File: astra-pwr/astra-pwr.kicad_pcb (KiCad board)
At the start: 2 copper layers, 66.4 x 44 mm, 45 parts, among them J1 12V_IN, J2 RPI_PWR, J3 MISC_OUT, J4 STATUS_LED, U1 LMR54410DBVR, U2 TPS563240DDC, U3 LM321MF, U4 LM321MF, U5 LM321MF

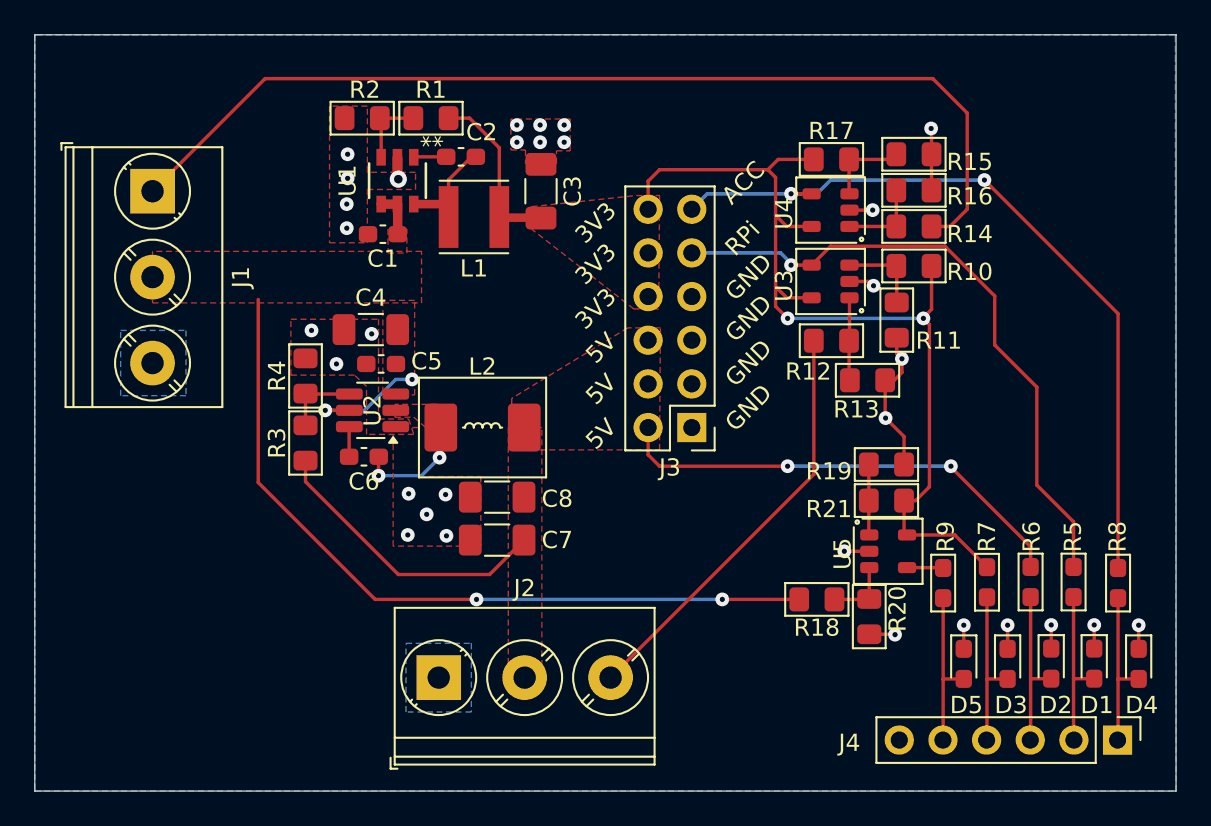
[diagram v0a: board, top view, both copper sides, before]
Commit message: Touchups on power board size
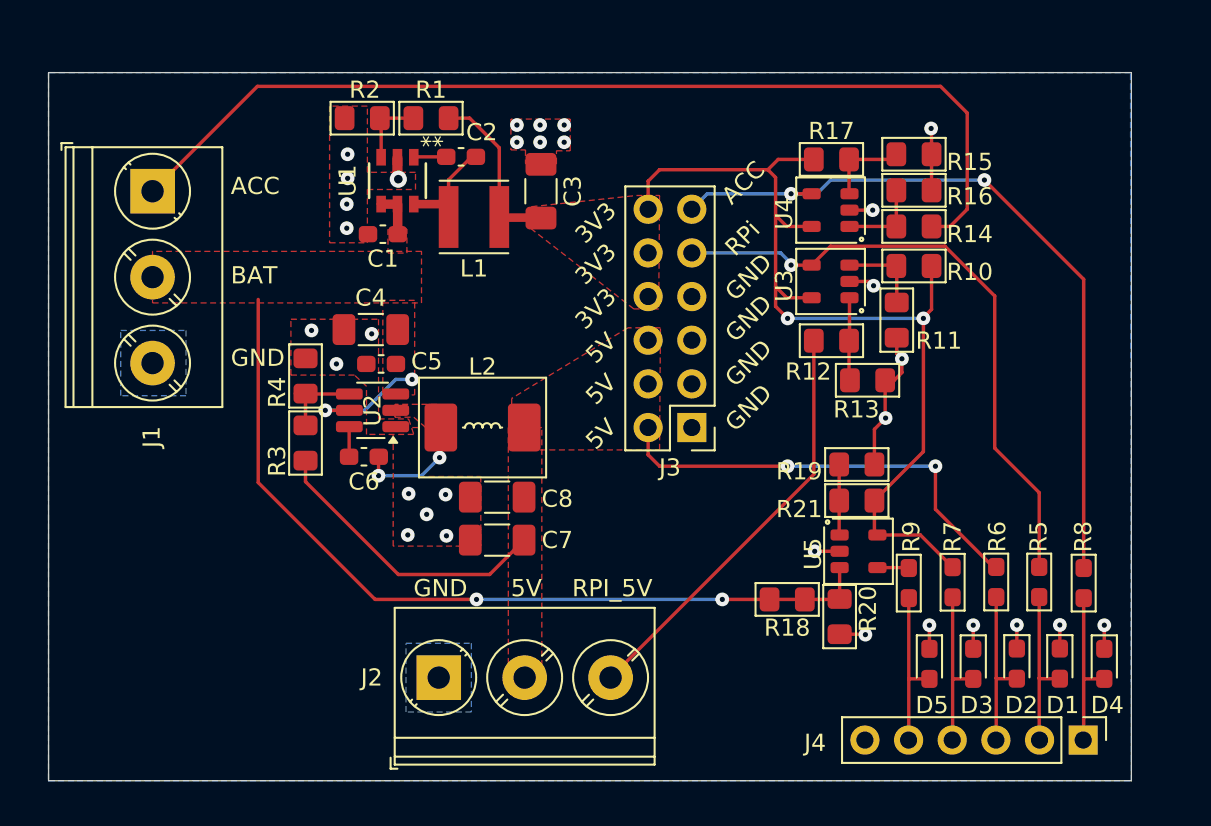
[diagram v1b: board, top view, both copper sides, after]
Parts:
- moved D1 2.00 mm to (97.2, 75.8)
- moved D2 2.00 mm to (94.7, 75.8)
- moved D3 2.00 mm to (92.2, 75.8)
- moved D4 2.00 mm to (99.8, 75.8)
- moved D5 2.00 mm to (89.7, 75.8)
- moved J4 2.00 mm to (98.6, 80.2)
- moved R5 2.00 mm to (96.0, 71.0)
- moved R6 2.00 mm to (93.5, 71.0)
- moved R7 2.00 mm to (91.0, 71.0)
- moved R8 2.00 mm to (98.6, 71.1)
- moved R9 2.00 mm to (88.5, 71.1)
- moved R19 1.73 mm to (85.4, 64.2)
- moved R20 1.73 mm to (84.4, 73.0)
- moved R21 1.73 mm to (85.4, 66.3)
- moved R18 1.72 mm to (81.4, 72.0)
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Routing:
- net 5V: track 44.3 -> 43.1 mm
- net RPI_PWR: track 37.2 -> 36.4 mm
- net ACC_UP: track 44.9 -> 44.1 mm
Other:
- board size 66.4 x 44 mm -> 63 x 41.2 mm
- board text added: "BAT"
- board text added: "RPI_5V"

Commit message: Feedback Secilio 2
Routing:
- net 3V3: track 66.0 -> 63.9 mm
- net BAT: track 55.0 -> 56.3 mm
- net GND: track 26.5 -> 25.3 mm, vias 31 -> 71
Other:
- board text added: "*"
